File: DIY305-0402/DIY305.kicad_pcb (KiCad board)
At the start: 2 copper layers, 9.8 x 18.5 mm, 37 parts, among them J3 Conn_01x14

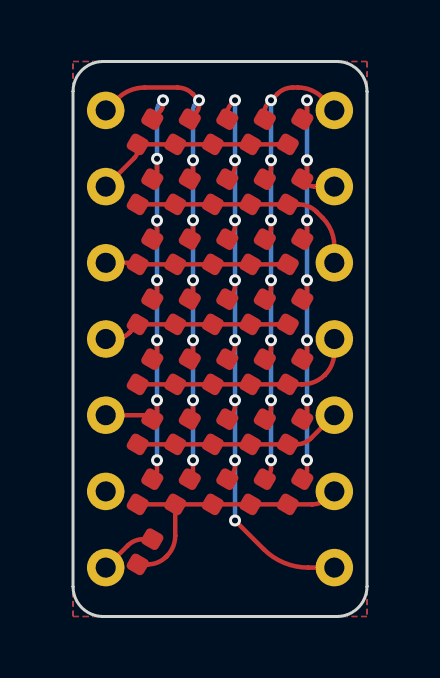
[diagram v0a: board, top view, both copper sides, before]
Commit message: added castellations to the DIY305
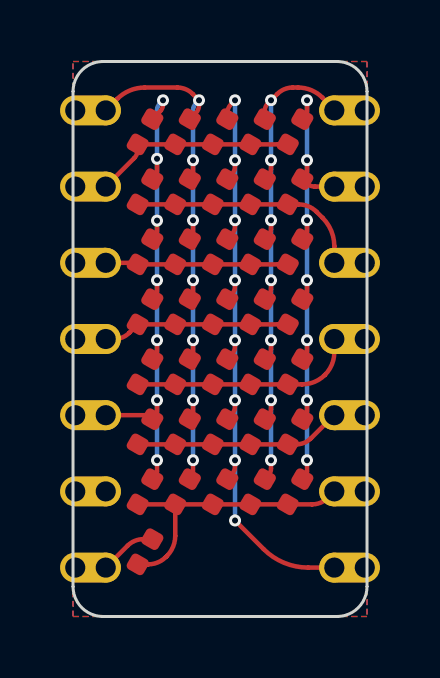
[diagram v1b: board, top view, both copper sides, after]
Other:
- board text added: "DIY-305 Designed by Ru-Pirie and Envious.Design"
- board text removed: "Ru-Pirie"
